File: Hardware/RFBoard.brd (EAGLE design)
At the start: 100 x 100 mm, 375 parts, among them IC1 HMC1097, IC10 NCP702-1.8, IC11 TPS42951, IC12 MCP4812, IC13 STM32F030C8T, IC14 LT5560, IC15 ADF4360, IC16 HMC284, IC17 HMC284, IC18 NCP702-3.3, IC19 NCP702-3.3, IC2 MAX2871, IC20 LT1395, IC21 MAADSS0008, IC22 MAADSS0008, IC23 MAADSS0008, IC24 RFSA2033, IC25 MMG3H21NT1, IC26 MMG3H21NT1, IC27 HMC1021, IC28 MCP4812, IC29 NCP702-3.3, IC3 AP2114HA-3.3, IC31 QPC6064, IC32 QPC6064, IC4 NCP702-3.3, IC5 NCP702-3.3, IC6 MAX5873, IC7 NCP702-1.8, IC8 NCP702-3.3, IC9 NCP702-3.3, Q1 BSS123, Q2 BSS123, Q3 BSS123, Q4 BSS123, Q5 BSS123, Q6 BSS84, U1 6SLX9TQG144, U4 W25Q16BVSN, X1 out

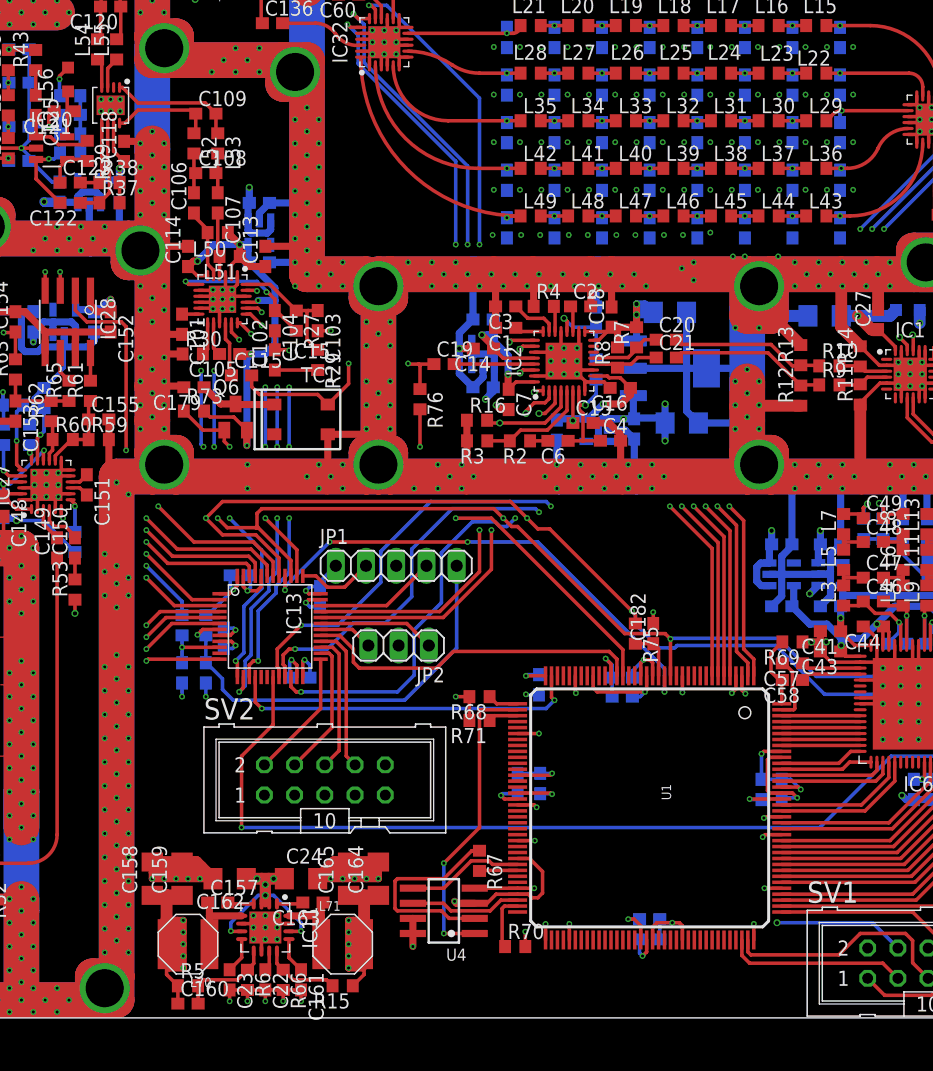
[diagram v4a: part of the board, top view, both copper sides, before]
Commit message: Via stitching, missing connections, FPGA pins to FFC connector
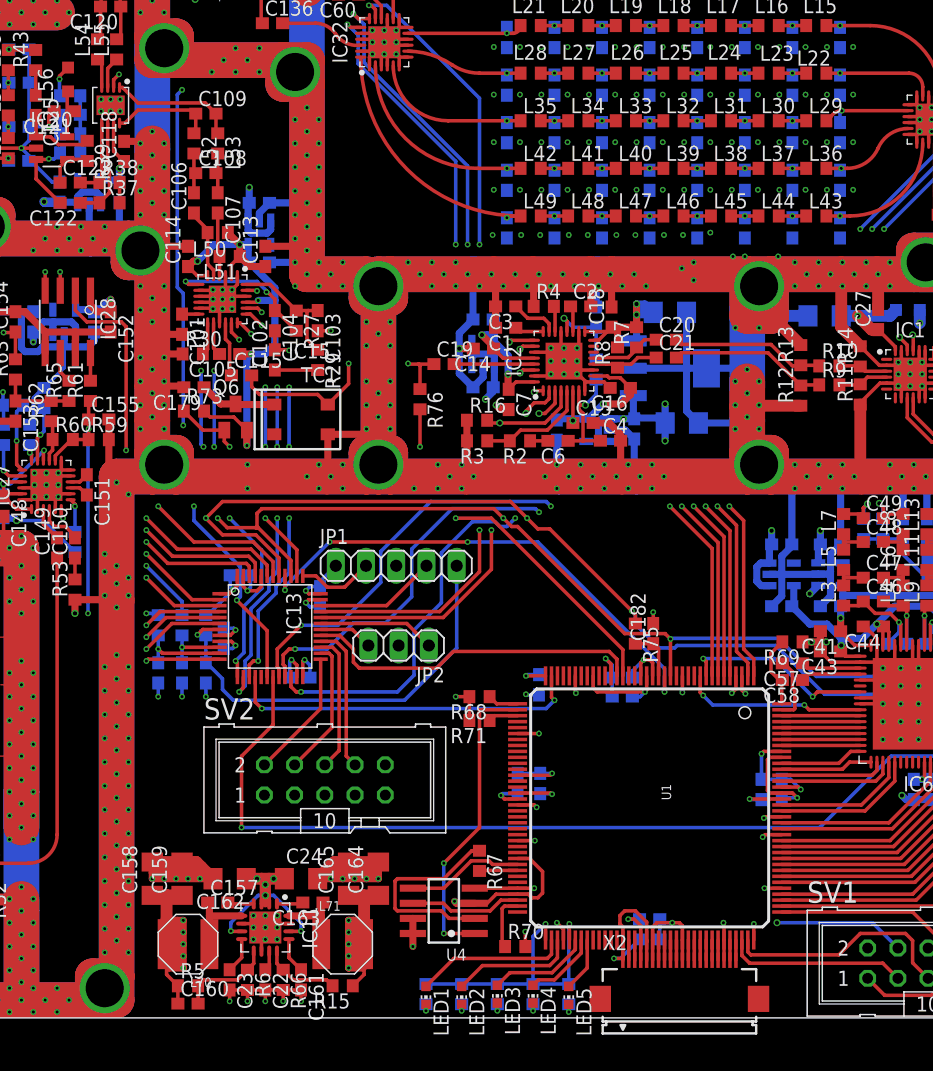
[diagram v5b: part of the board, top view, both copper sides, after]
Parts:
- added C183: 100n, rcl:C0603
- added LED1, LED2, LED3, LED4, LED5: (no value), led:CHIP-LED0603
- added R77: 10k, resistor:R0603
- added R78, R79, R80, R81, R82: 220, resistor:R0603
- added X2: FH12-20S-0.5SH, con-hirose:FH12-20S-0.5SH
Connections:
- new net N$157: C183.1, IC13.11, R77.2
- new net N$193: U1.P87, X2.2
- new net N$194: U1.P88, X2.3
- new net N$195: U1.P92, X2.7
- new net N$196: U1.P93, X2.8
- new net N$197: U1.P94, X2.9
- new net N$198: U1.P95, X2.10
- new net N$199: U1.P97, X2.12
- new net N$200: U1.P98, X2.13
- new net N$201: U1.P99, X2.14
- new net N$202: U1.P101, X2.16
- new net N$203: U1.P102, X2.17
- new net N$204: U1.P104, X2.19
- new net N$205: U1.P105, X2.20
- new net N$206: LED1.C, R78.2
- new net N$207: LED2.C, R79.2
- new net N$208: LED3.C, R80.2
- new net N$209: LED4.C, R81.2
- new net N$210: LED5.C, R82.2
- new net N$211: LED1.A, U1.P74
- new net N$212: LED2.A, U1.P75
- new net N$213: LED3.A, U1.P78
- new net N$214: LED4.A, U1.P79
- new net N$215: LED5.A, U1.P80
- new net RMSOUT: C155.1, IC27.14, R59.1, R60.2, R61.1, R77.1
- net +3V3: now also U1.P103, U1.P76, U1.P86, X2.1, X2.18, X2.5
- net DORI: now also U1.P9
- net GND: now also C183.2, IC6.40, R78.1, R79.1, R80.1, R81.1, R82.1, X2.11, X2.6
- net MIX_EN: now also IC13.18
- net N$162: now also U1.P100, X2.15; no longer C155.1, IC27.14, R59.1, R60.2, R61.1
- net SELIQ: now also U1.P10
- net VCCINT: now also X2.4
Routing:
- net MIX_EN: track 0.00 -> 60.0 mm, vias 0 -> 5
- net GND: track 2236.7 -> 2267.6 mm, vias 995 -> 996
- net RMSOUT: track 0.00 -> 28.9 mm, vias 0 -> 3
- net DORI: track 0.00 -> 16.2 mm, vias 0 -> 2
- net SELIQ: track 0.00 -> 15.4 mm, vias 0 -> 2
- net +3V3: track 102.8 -> 118.3 mm, vias 24 -> 26
- net N$211: track 0.00 -> 12.9 mm
- net N$212: track 0.00 -> 10.5 mm
- net N$213: track 0.00 -> 8.59 mm
- net N$157: track 0.00 -> 7.59 mm, vias 0 -> 1
- net N$214: track 0.00 -> 6.27 mm
- net N$162: track 7.10 -> 1.70 mm
- net N$215: track 0.00 -> 4.54 mm
- net VCCINT: track 42.9 -> 44.6 mm
- net N$205: track 0.00 -> 1.70 mm
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
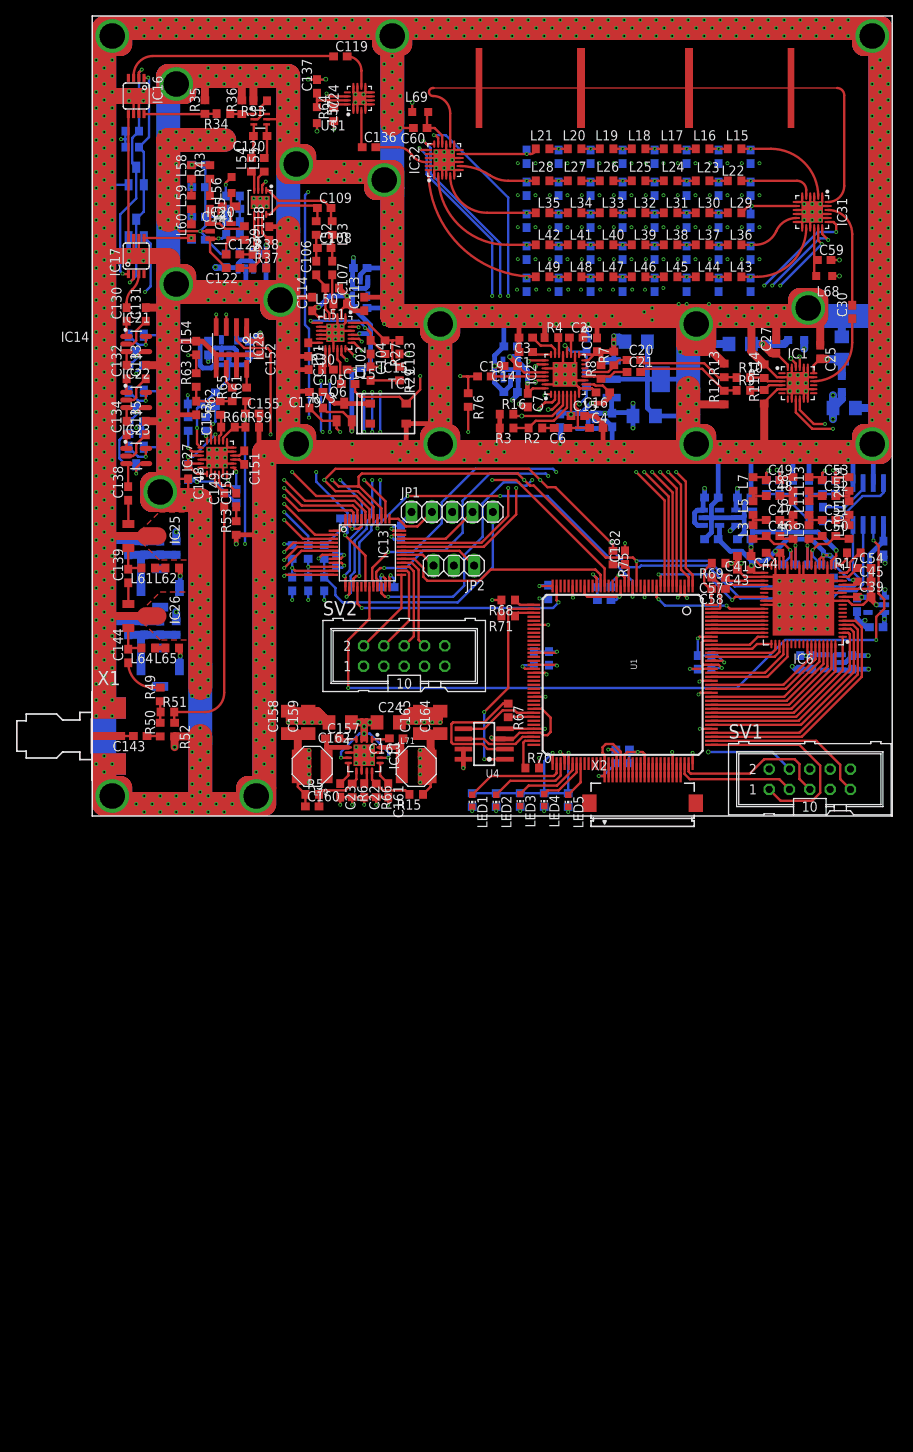
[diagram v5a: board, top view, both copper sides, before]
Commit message: Silkscreen, MOD_EN wire
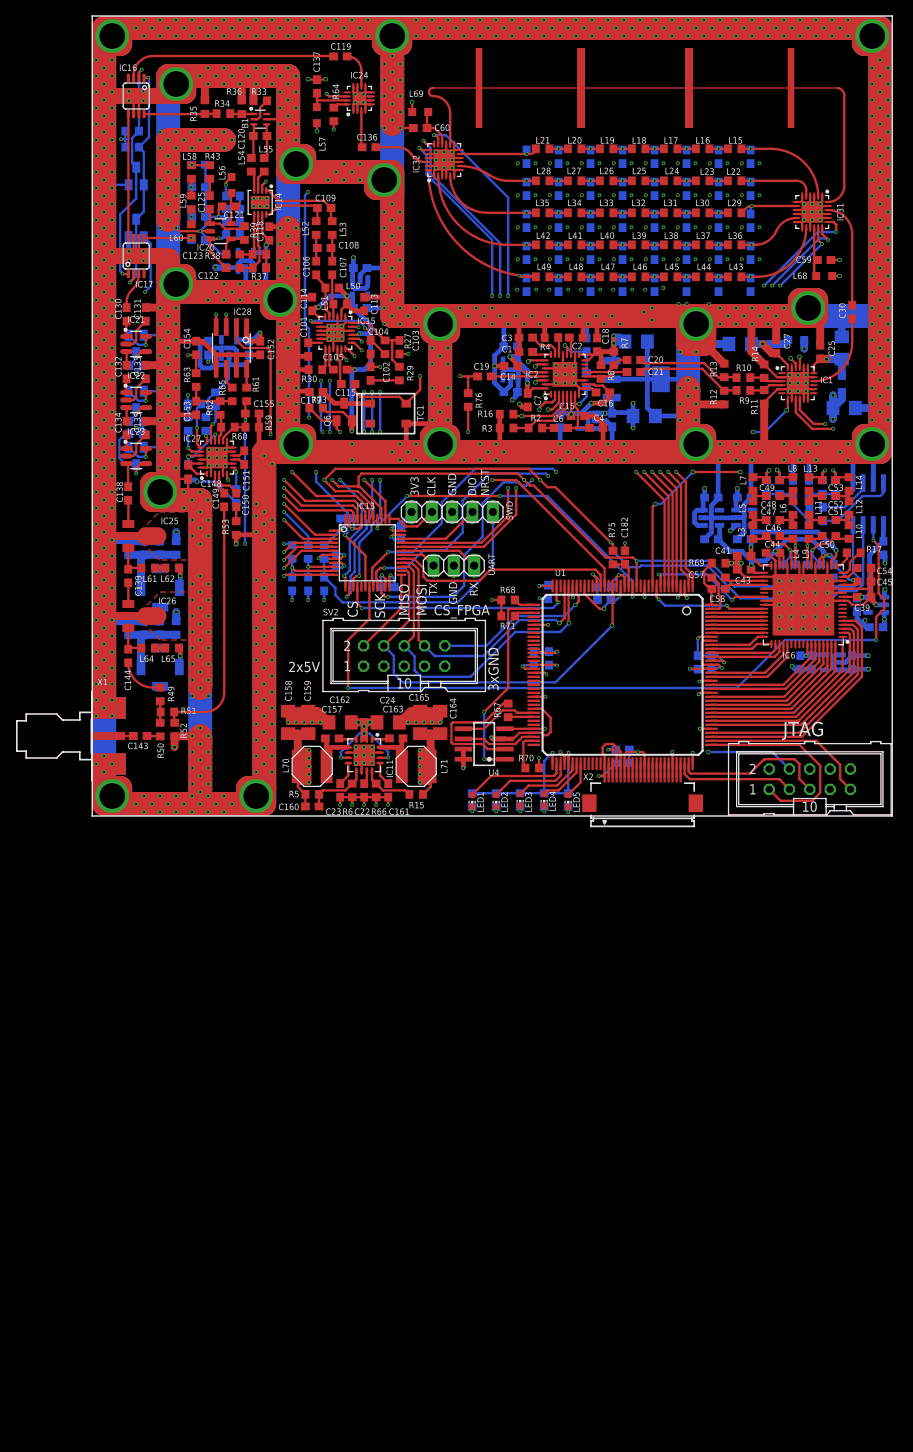
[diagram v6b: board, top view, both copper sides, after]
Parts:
- renumbered JP1 to SWD, JP2 to UART, SV1 to JTAG, U$1 to B1
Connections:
- net N$178 renamed RX
- net N$179 renamed TX
- net N$180 renamed SWCLK
- net N$182 renamed SWDIO
- net N$183 renamed NRST
- net N$185 renamed CS
- removed net N$186: IC13.28, SV2.8
- removed net N$187: IC13.27, SV2.6
- removed net N$188: IC13.26, SV2.4
- new net CS_FPGA: SV2.10, U1.P30
- new net MISO: IC13.27, SV2.6, U1.P32
- new net MOSI: IC13.28, SV2.8, U1.P33
- new net SCK: IC13.26, SV2.4, U1.P21
- net /MOD_EN: now also U1.P11
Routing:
- net SCK: track 0.00 -> 51.1 mm, vias 0 -> 1
- net MISO: track 0.00 -> 42.3 mm, vias 0 -> 1
- net /MOD_EN: track 0.00 -> 37.8 mm, vias 0 -> 5
- net MOSI: track 0.00 -> 36.7 mm, vias 0 -> 1
- net CS_FPGA: track 0.00 -> 21.1 mm, vias 0 -> 1
- net N$186: track 12.3 -> 0.00 mm
- net N$187: track 11.6 -> 0.00 mm
- net N$188: track 11.5 -> 0.00 mm
- net N$85: track 20.1 -> 21.0 mm
- net VCCINT: track 44.6 -> 44.8 mm, vias 9 -> 10
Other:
- board text added: "+5V"
- board text added: "1MHz-2.5GHz"
- board text added: "2x5V"
- board text added: "3V3"
- board text added: "3xGND"
- board text added: "CLK"
- board text added: "CS"
- board text added: "CS_FPGA"
- board text added: "DIO"
- board text added: "GND"
- board text added: "MISO"
- board text added: "MOSI"
- board text added: "NRST"
- board text added: "RX"
- board text added: "Rev. A"
- board text added: "SCK"
- board text added: "Signalgenerator"
- board text added: "TX"
- board text added: "github.com/jankae/Signalgenerator"
